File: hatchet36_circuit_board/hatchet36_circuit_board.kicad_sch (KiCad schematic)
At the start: 102 parts

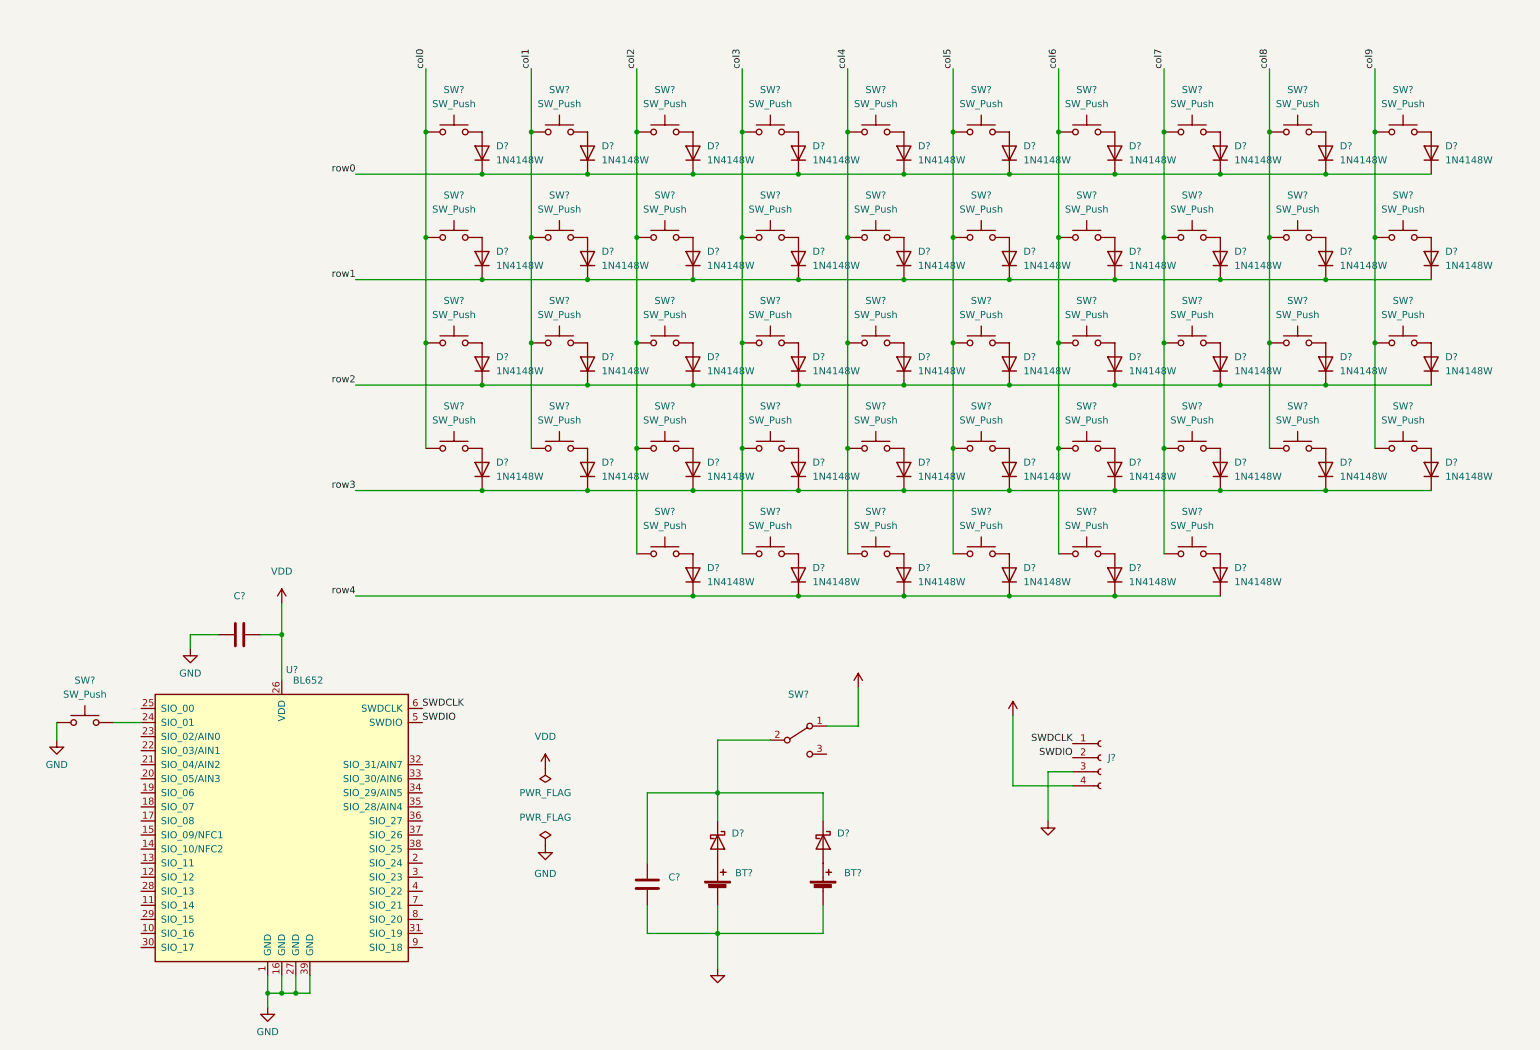
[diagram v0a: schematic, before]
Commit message: annotate schematic symbol
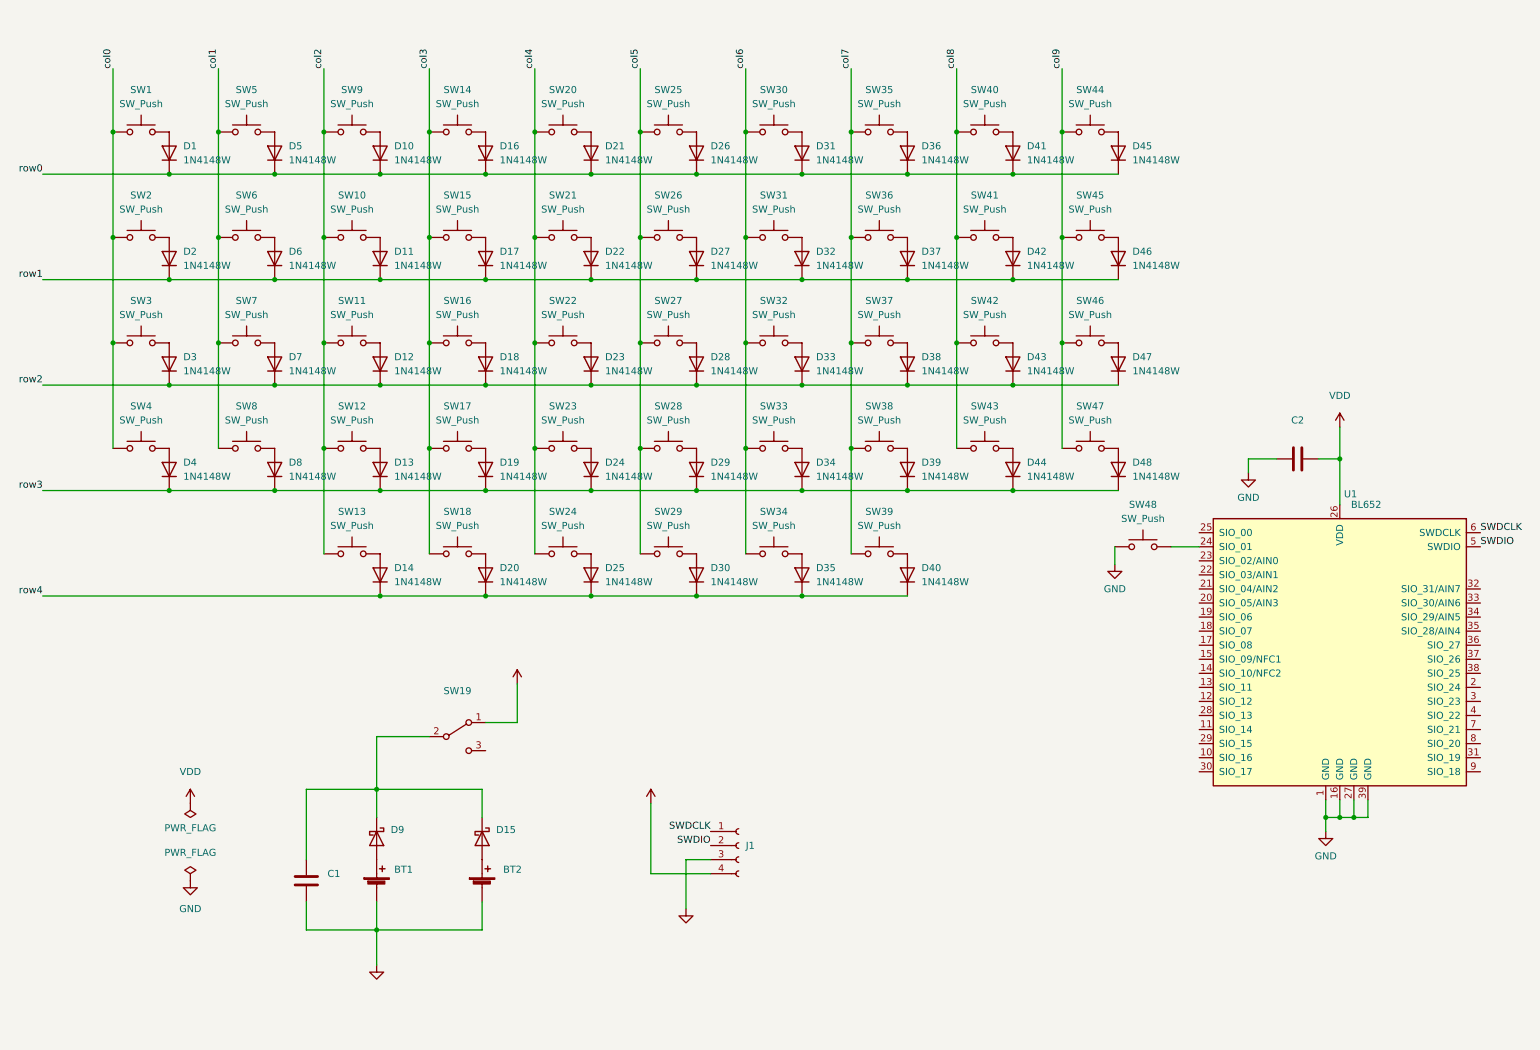
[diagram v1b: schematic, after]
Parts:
- gave numbers to parts that had none: 102
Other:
- moved on the sheet: BT1, BT2, C1, C2, D1, D10, D11, D12, D13, D14, D15, D16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

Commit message: add footprint of bl652 which has long pad
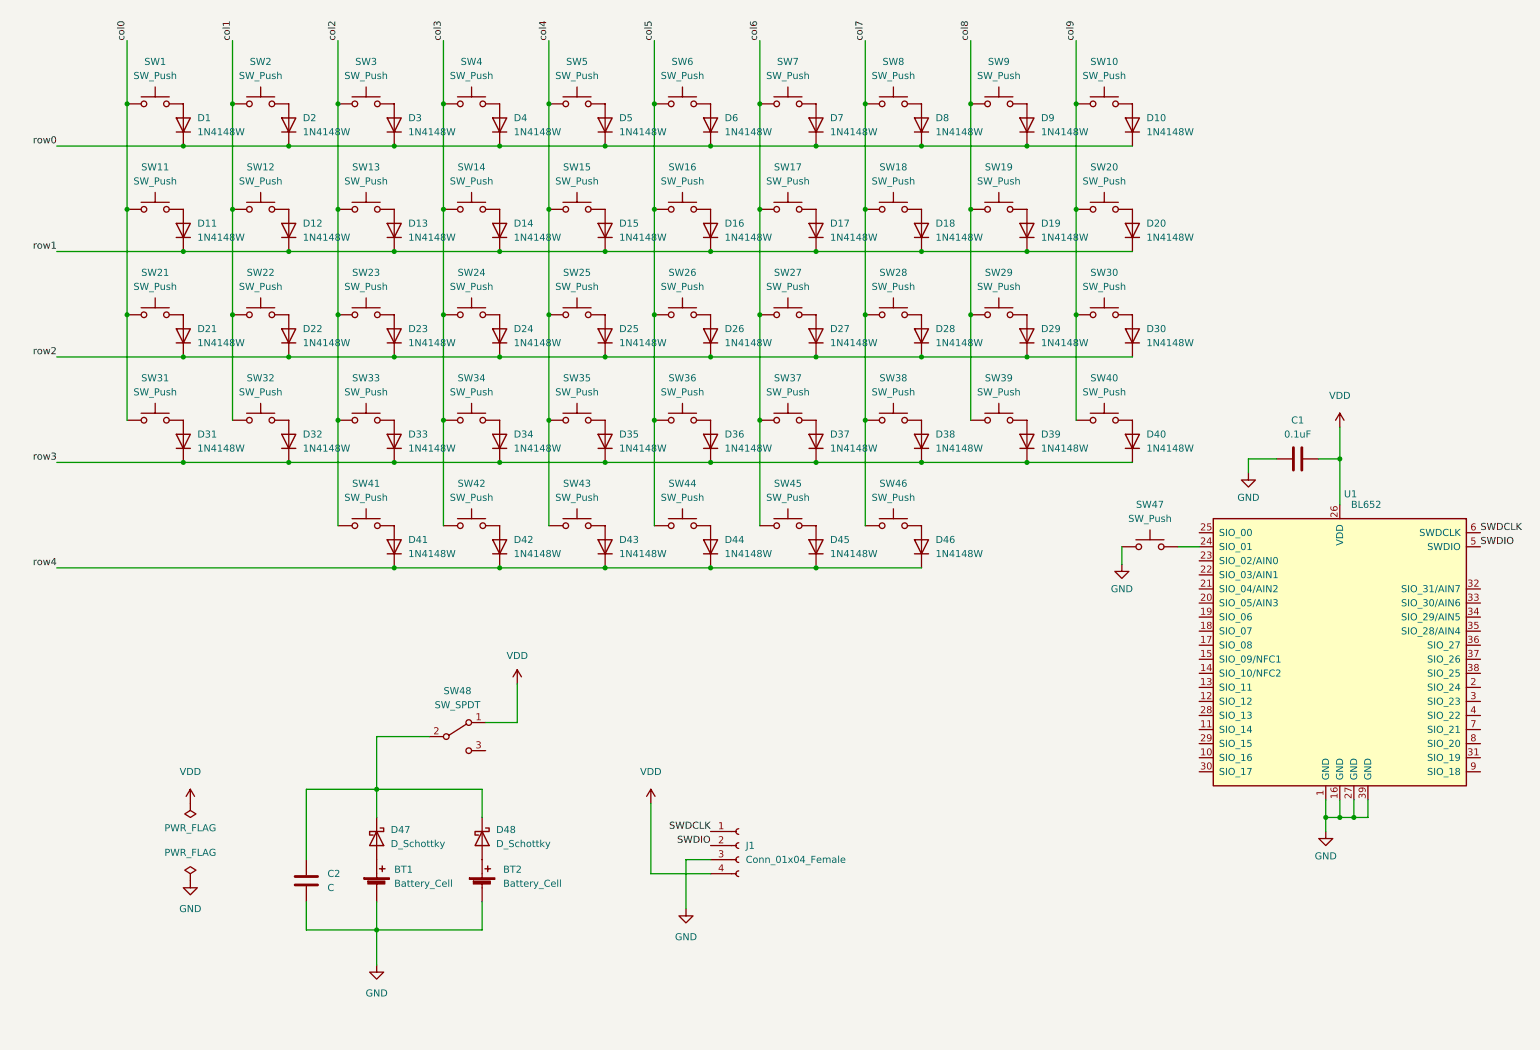
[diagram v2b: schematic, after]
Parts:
- BT1, BT2: value (none) -> Battery_Cell; footprint (none) -> Battery:Battery_Panasonic_CR1632-V1AN_Vertical_CircularHoles
- C1: renamed from C2; value (none) -> 0.1uF
- C2: renamed from C1; value (none) -> C
- D47: renamed from D9; value (none) -> D_Schottky
- D48: renamed from D15; value (none) -> D_Schottky
- J1: value (none) -> Conn_01x04_Female
- SW48: renamed from SW19; value (none) -> SW_SPDT
- renumbered D45 to D10, D2 to D11, D6 to D12, D11 to D13, D17 to D14, D22 to D15, D27 to D16, D32 to D17, D37 to D18, D42 to D19, D5 to D2, D46 to D20, D3 to D21, D7 to D22, D12 to D23, D18 to D24, D23 to D25, D28 to D26, D33 to D27, D38 to D28, D43 to D29, D10 to D3, D47 to D30, D4 to D31, D8 to D32, D13 to D33, D19 to D34, D24 to D35, D29 to D36, D34 to D37, D39 to D38, D44 to D39, D16 to D4, D48 to D40, D14 to D41, D20 to D42, D25 to D43, D30 to D44, D35 to D45, D40 to D46, D21 to D5, D26 to D6, D31 to D7, D36 to D8, D41 to D9, SW44 to SW10, SW2 to SW11, SW6 to SW12, SW10 to SW13, SW15 to SW14, SW21 to SW15, SW26 to SW16, SW31 to SW17, SW36 to SW18, SW41 to SW19, SW5 to SW2, SW45 to SW20, SW3 to SW21, SW7 to SW22, SW11 to SW23, SW16 to SW24, SW22 to SW25, SW27 to SW26, SW32 to SW27, SW37 to SW28, SW42 to SW29, SW9 to SW3, SW46 to SW30, SW4 to SW31, SW8 to SW32, SW12 to SW33, SW17 to SW34, SW23 to SW35, SW28 to SW36, SW33 to SW37, SW43 to SW39, SW14 to SW4, SW47 to SW40, SW13 to SW41, SW18 to SW42, SW24 to SW43, SW29 to SW44, SW34 to SW45, SW39 to SW46, SW48 to SW47, SW20 to SW5, SW25 to SW6, SW30 to SW7, SW35 to SW8, SW40 to SW9
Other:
- moved on the sheet: D1, D10, D11, D12, D13, D14, D15, D16, D17, D18, D19, D2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

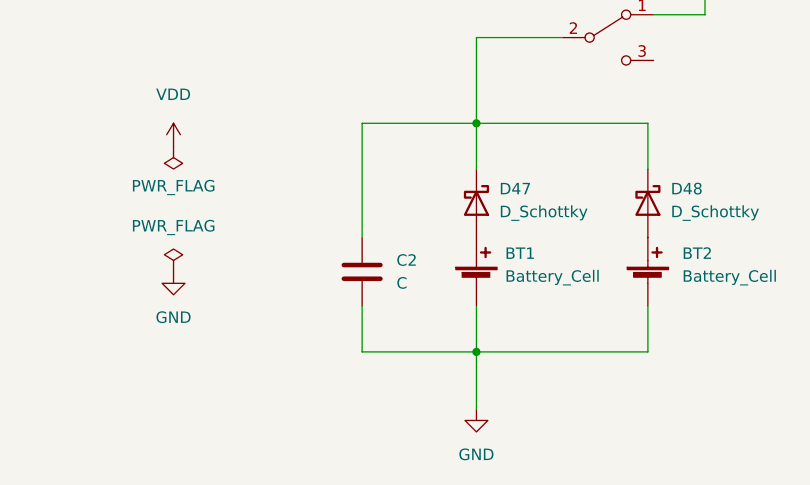
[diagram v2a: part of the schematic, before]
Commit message: assignment some footprint
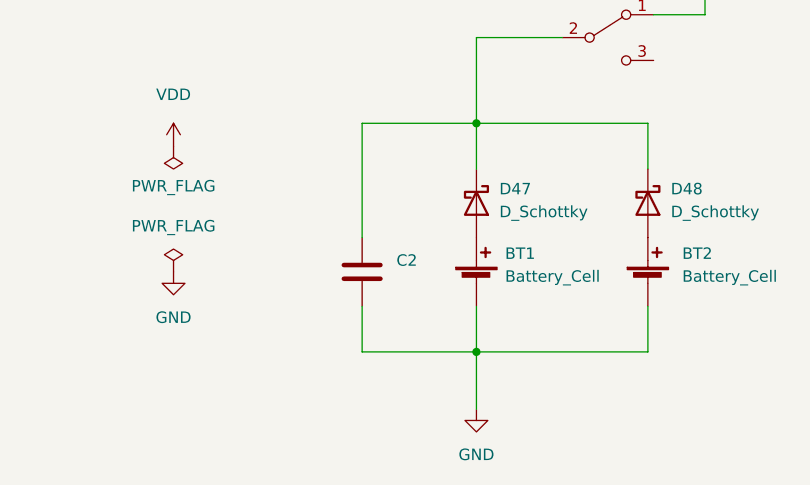
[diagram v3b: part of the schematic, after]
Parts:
- C2: value C -> (none)
- U1: footprint RF_Module:Laird_BL652 -> (none)
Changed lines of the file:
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@@
       (effects (font (size 1.27 1.27)) (justify left))
     )
-    (property "Footprint" "RF_Module:Laird_BL652" (id 2) (at 252.095 158.75 0)
+    (property "Footprint" "" (id 2) (at 252.095 158.75 0)
       (effects (font (size 1.27 1.27)) hide)
     )
@@
       (effects (font (size 1.27 1.27)) (justify left))
     )
-    (property "Value" "C" (id 1) (at 69.215 169.5449 0)
+    (property "Value" "" (id 1) (at 69.215 169.5449 0)
       (effects (font (size 1.27 1.27)) (justify left))
     )
@@
     )
     (path "/860000f7-cb11-4cf7-9dab-9773b2e1b109"
-      (reference "C1") (unit 1) (value "0.1uF") (footprint "")
+      (reference "C1") (unit 1) (value "0.1uF") (footprint "Capacitor_SMD:C_0805_2012Metric_Pad1.18x1.45mm_HandSolder")
     )
     (path "/f133eb4b-bea7-4a45-8bb5-e8a6319664c0"
-      (reference "C2") (unit 1) (value "C") (footprint "")
+      (reference "C2") (unit 1) (value "100uF") (footprint "Capacitor_SMD:C_1206_3216Metric_Pad1.33x1.80mm_HandSolder")
     )
     (path "/9df78b20-7bdb-4d86-a1fa-287b83d1fff1"
@@
     )
     (path "/36c7a529-9c48-4cc8-b39d-47cdef98a63f"
-      (reference "D47") (unit 1) (value "D_Schottky") (footprint "")
+      (reference "D47") (unit 1) (value "D_Schottky") (footprint "Diode_SMD:D_SOD-323")
     )
     (path "/ee9248ee-b382-4dfd-97fe-fd6ed5de3832"
-      (reference "D48") (unit 1) (value "D_Schottky") (footprint "")
+      (reference "D48") (unit 1) (value "D_Schottky") (footprint "Diode_SMD:D_SOD-323")
     )
     (path "/f4b00c54-9ad1-49cc-a893-af751b7bbde3"
@@
     )
     (path "/73846744-8199-4c16-b04a-3244ef0b5a6a"
-      (reference "U1") (unit 1) (value "BL652") (footprint "RF_Module:Laird_BL652")
-    )
-  )
+      (reference "U1") (unit 1) (value "BL652") (footprint "locallib:Laird_BL652_LongPad")
+    )
+  )

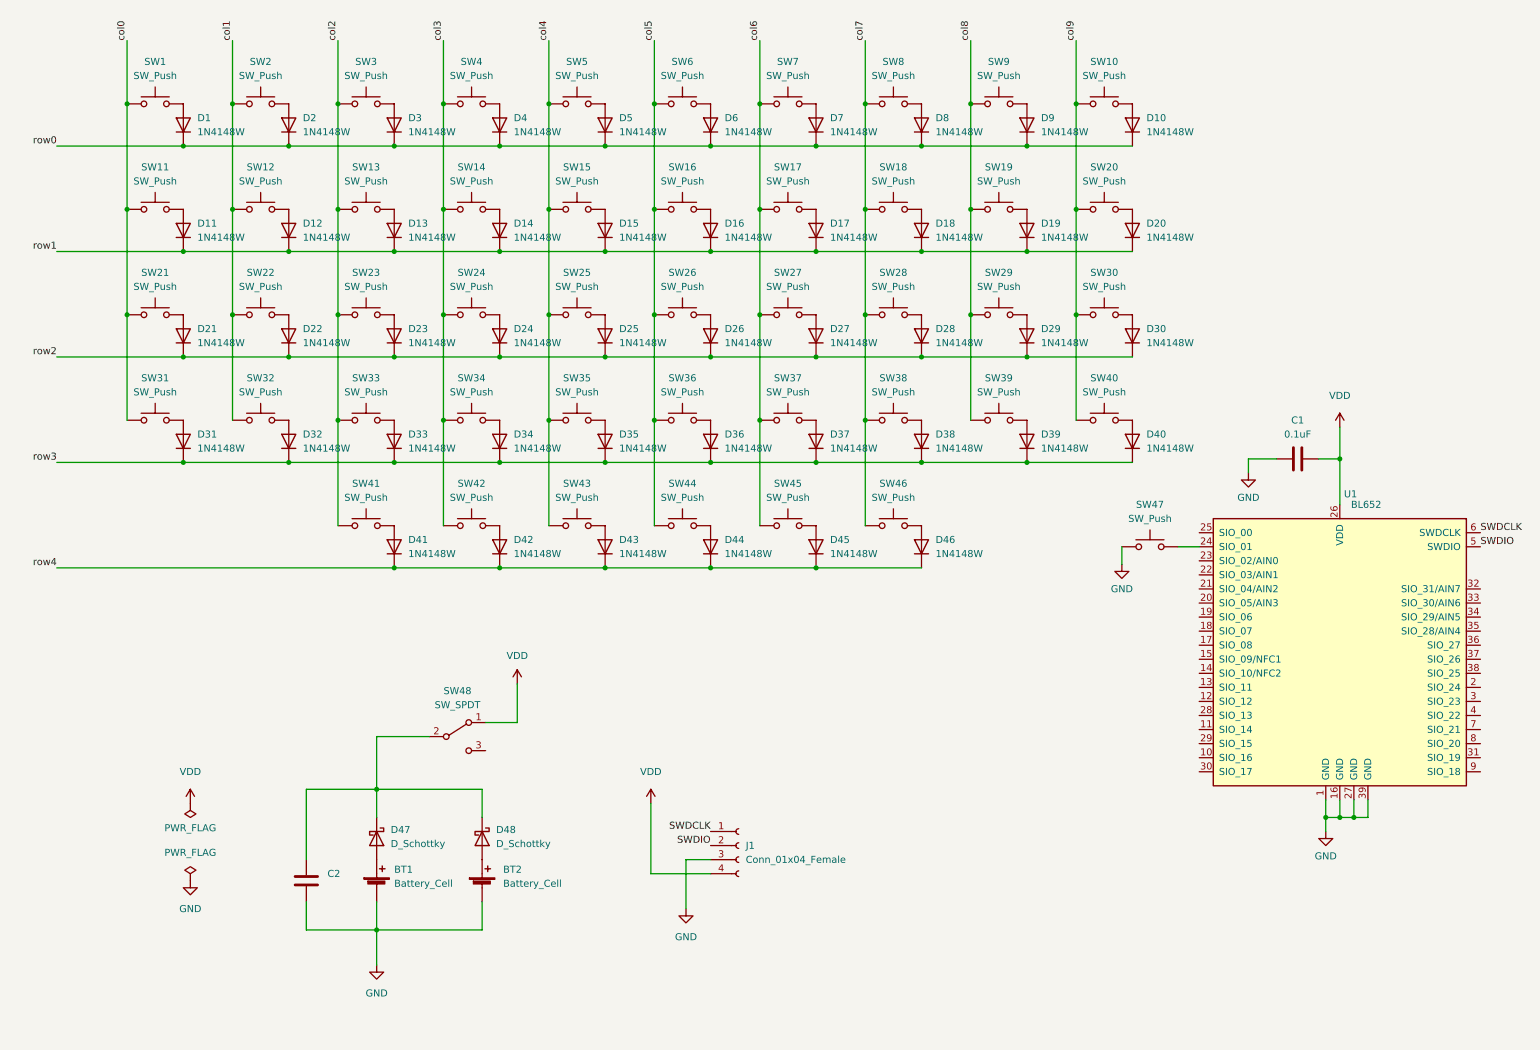
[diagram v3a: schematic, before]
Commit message: align keys
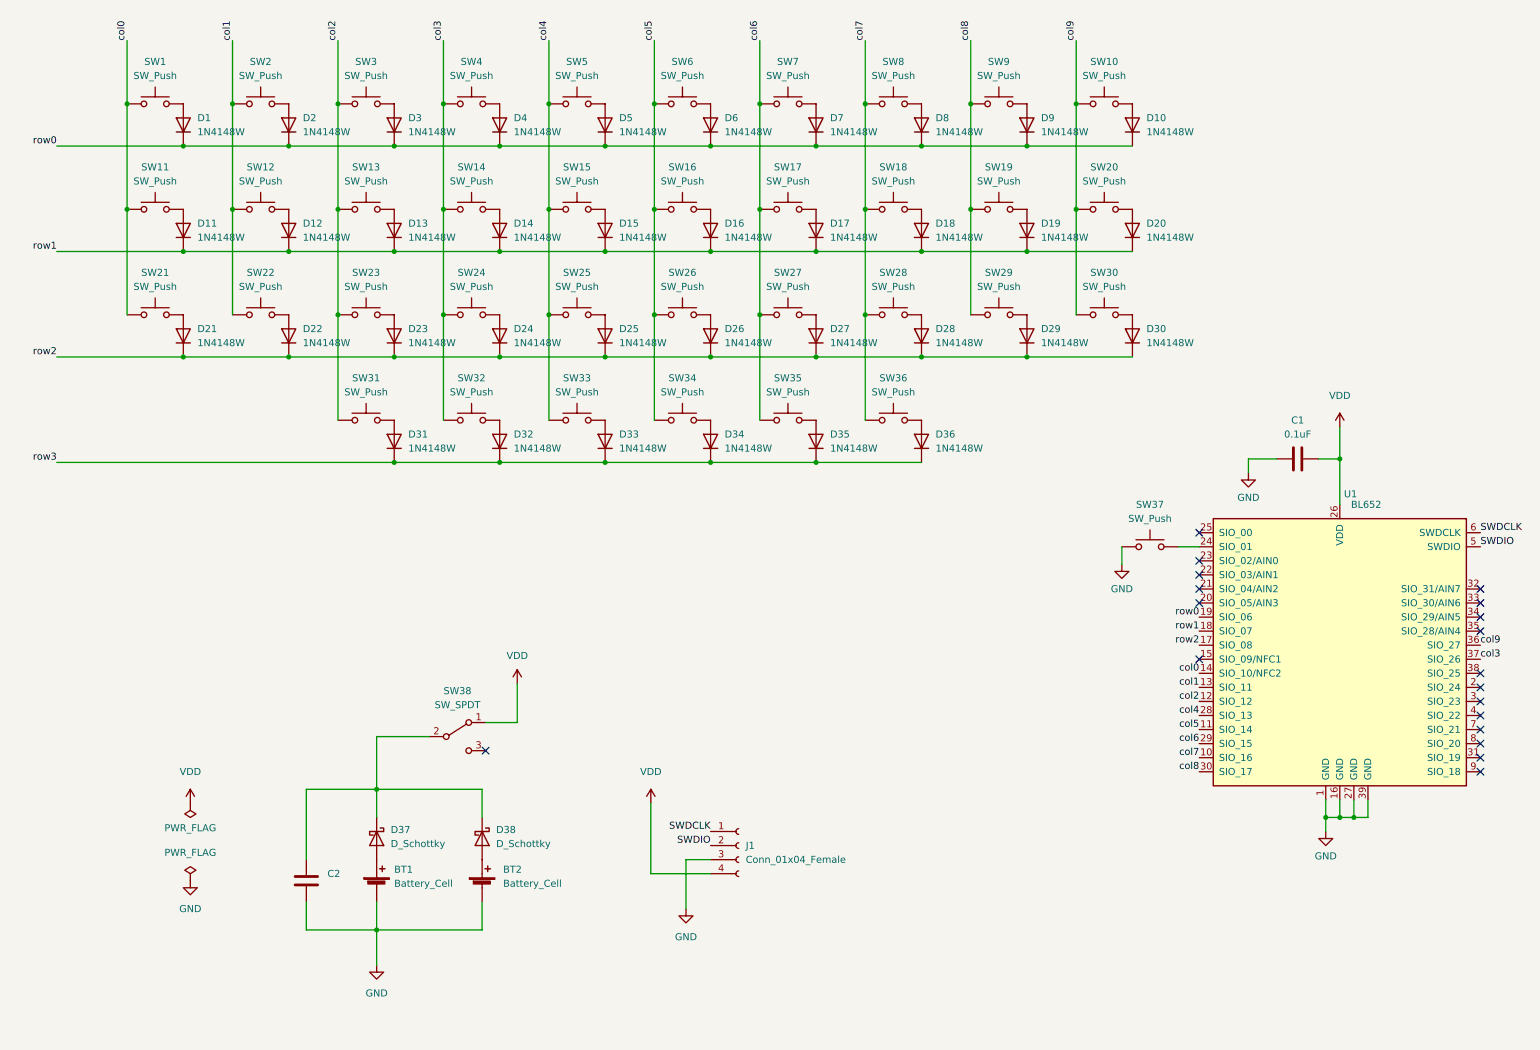
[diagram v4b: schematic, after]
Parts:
- removed D31, D32, D39, D40, D41, D42, D43, D44, D45, D46: 1N4148W, Diode_SMD:D_SOD-123, symbol Diode:1N4148W
- removed SW31, SW32, SW39, SW40, SW41, SW42, SW43, SW44, SW45, SW46: SW_Push, symbol Switch:SW_Push
- BT1, BT2: footprint Battery:Battery_Panasonic_CR1632-V1AN_Vertical_CircularHoles -> (none)
- renumbered D33 to D31, D34 to D32, D35 to D33, D36 to D34, D37 to D35, D38 to D36, D47 to D37, D48 to D38, SW33 to SW31, SW34 to SW32, SW35 to SW33, SW36 to SW34, SW37 to SW35, SW38 to SW36, SW47 to SW37, SW48 to SW38
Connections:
- net col0: now also U1.14 (SIO_10/NFC2)
- net col1: now also U1.13 (SIO_11)
- net col2: now also U1.12 (SIO_12)
- net col3: now also U1.37 (SIO_26)
- net col4: now also U1.28 (SIO_13)
- net col5: now also U1.11 (SIO_14)
- net col6: now also U1.29 (SIO_15)
- net col7: now also U1.10 (SIO_16)
- net col8: now also U1.30 (SIO_17)
- net col9: now also U1.36 (SIO_27)
- net row0: now also U1.19 (SIO_06)
- net row1: now also U1.18 (SIO_07)
- net row2: now also U1.17 (SIO_08)
- no-connect marks 0 -> 19
